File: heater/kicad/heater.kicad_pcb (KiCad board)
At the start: 2 copper layers, 90 x 88.4 mm, 82 parts, among them J1 Conn_01x02_Pin, J2 Conn_01x02_Pin, J3 pcie_98, U1 OPA863SIDBVR, U10 B0509XT-1WR3, U11 ESD5344D-TP, U12 ESD5344D-TP, U13 XC6206P332MR, U2 OPA863SIDBVR, U3 LTC1968, U4 LTC1968, U5 OPA863SIDBVR, U6 OPA863SIDBVR, U7 LP2985-5.0, U8 ADS1115IDGS, U9 ISO1541

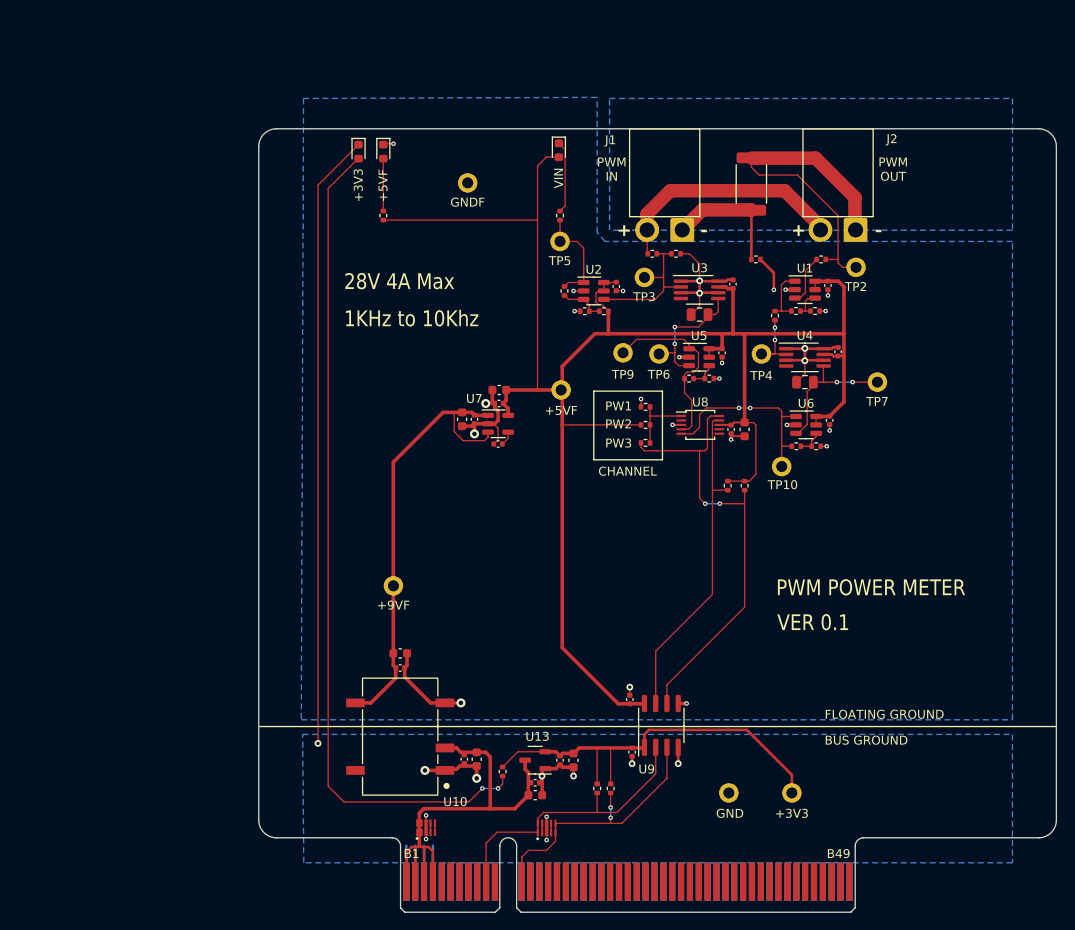
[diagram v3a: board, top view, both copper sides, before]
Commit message: Routed V2 of the heater board.
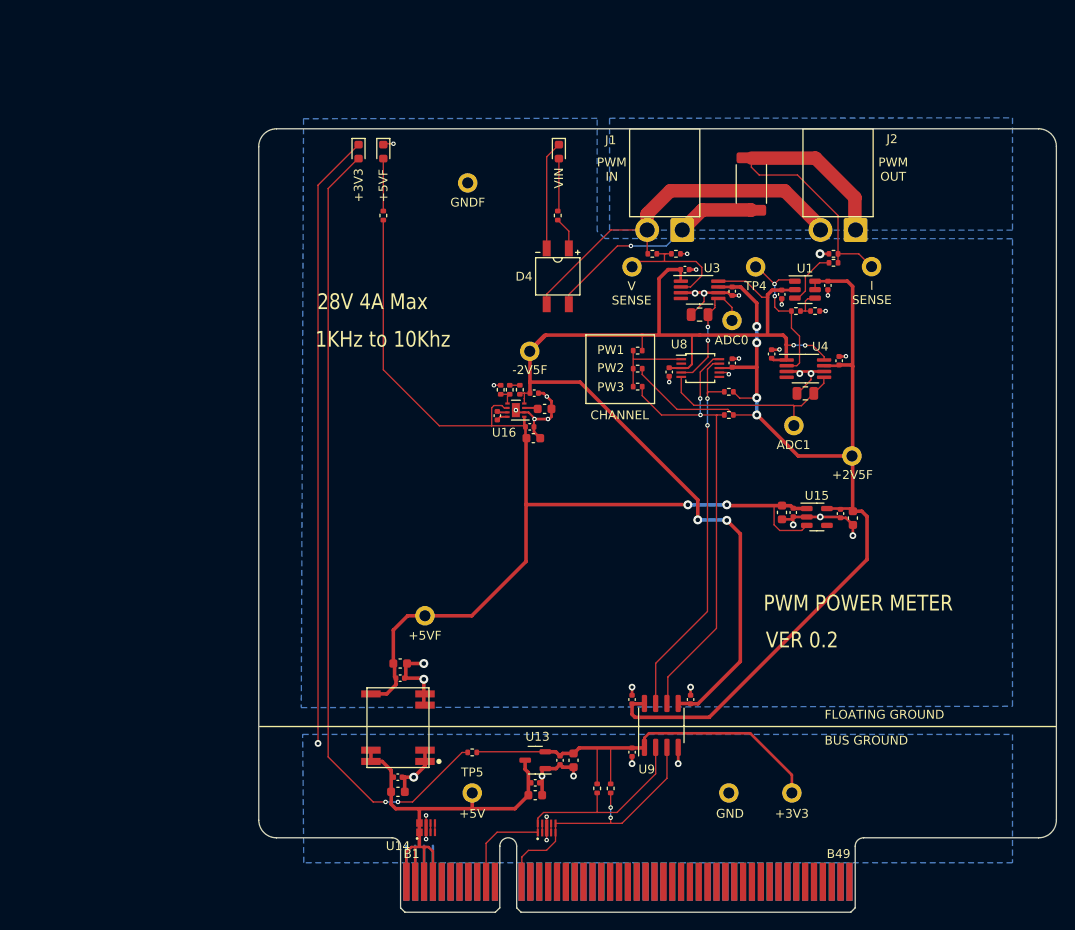
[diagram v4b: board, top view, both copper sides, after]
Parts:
- removed C10, C2: 100n, Capacitor_SMD:C_0402_1005Metric
- removed C11: 10n, Capacitor_SMD:C_0402_1005Metric
- removed C12: 10u, Capacitor_SMD:C_0603_1608Metric
- removed C14: 100n 16V, Capacitor_SMD:C_0402_1005Metric
- removed C15: 10u 16V, Capacitor_SMD:C_0603_1608Metric
- removed D2: RED, LED_SMD:LED_0603_1608Metric
- removed R11: 1M, Resistor_SMD:R_0402_1005Metric
- removed R13: 5K1, Resistor_SMD:R_0402_1005Metric
- removed R14, R16: 30K, Resistor_SMD:R_0402_1005Metric
- removed R15, R17: 10K, Resistor_SMD:R_0402_1005Metric
- removed R7: 50K, Resistor_SMD:R_0402_1005Metric
- removed R8: 2K, Resistor_SMD:R_0402_1005Metric
- removed TP10, TP9: TestPoint, common:Test_Pad
- removed U10: B0509XT-1WR3, heater:Converter_DCDC
- removed U2, U5, U6: OPA863SIDBVR, Package_TO_SOT_SMD:TSOT-23-6
- removed U7: LP2985-5.0, Package_TO_SOT_SMD:SOT-23-5
- added C26: 10u, Capacitor_SMD:C_0603_1608Metric, F.Cu at (38.9, -44.5)
- added C27: 100n, Capacitor_SMD:C_0402_1005Metric, F.Cu at (37.5, -45.0)
- added C28: 100n, Capacitor_SMD:C_0402_1005Metric, F.Cu at (32.2, -45.1)
- added C29: 10u, Capacitor_SMD:C_0603_1608Metric, F.Cu at (30.9, -45.1)
- added C30: 4u7, Capacitor_SMD:C_0603_1608Metric, F.Cu at (4.10, -56.8)
- added C31: 1u, Capacitor_SMD:C_0402_1005Metric, F.Cu at (2.93, -58.6)
- added C32: 1u, Capacitor_SMD:C_0402_1005Metric, F.Cu at (-1.23, -56.0)
- added C33: 10u, Capacitor_SMD:C_0603_1608Metric, F.Cu at (2.83, -53.5)
- added C34: 100n, Capacitor_SMD:C_0402_1005Metric, F.Cu at (2.42, -54.8)
- added C35: 100n, Capacitor_SMD:C_0402_1005Metric, F.Cu at (20.6, -24.0)
- added C37: 100n, Capacitor_SMD:C_0402_1005Metric, F.Cu at (18.2, -61.0)
- added D4: MBS10S, common:Diode_Bridge_MBS10, F.Cu at (5.59, -71.8)
- added D5: RED, LED_SMD:LED_0603_1608Metric, F.Cu at (5.71, -85.8)
- added R26: 200K, Resistor_SMD:R_0402_1005Metric, F.Cu at (1.31, -59.0)
- added R27: 200K, Resistor_SMD:R_0402_1005Metric, F.Cu at (-0.85, -59.0)
- added R28: 10K, Resistor_SMD:R_0402_1005Metric, F.Cu at (0.16, -59.0)
- added TP14: TestPoint, common:Test_Pad, F.Cu at (38.8, -51.5)
- added U14: B0505MT-1WR4, common:B0505MT-1WR4, F.Cu at (-12.4, -20.8)
- added U15: TPS7A2025PDBVR, Package_TO_SOT_SMD:SOT-23-5, F.Cu at (34.8, -44.6)
- added U16: LM27761, Package_SON:WSON-8-1EP_2x2mm_P0.5mm_EP0.9x1.6mm, F.Cu at (0.86, -56.7)
- C16: value 10u 16V -> 10u
- C17: value 100n 16V -> 100n
- C9: value 10u -> 100n; footprint Capacitor_SMD:C_0603_1608Metric -> Capacitor_SMD:C_0402_1005Metric
- R12: value 0R -> 10K
- R2: value 0R025 50ppm -> 0R025
- moved TP5 63.0 mm to (-4.06, -13.5)
- moved C9 33.7 mm to (30.9, -69.7), turned to -90 degrees
- moved R12 27.0 mm to (5.59, -78.6)
- moved TP3 25.7 mm to (41.0, -72.8)
- moved TP2 25.3 mm to (14.0, -72.8)
- moved TP7 10.6 mm to (32.2, -54.9)
- moved R21 10.6 mm to (24.9, -58.7), turned to 0 degrees
- moved C7 10.3 mm to (19.9, -72.5), turned to 0 degrees
- moved C8 9.95 mm to (29.7, -63.0), turned to 90 degrees
- moved TP4 9.85 mm to (27.9, -72.8)
- moved C22 9.62 mm to (-12.4, -13.6), turned to 180 degrees
- moved TP6 9.06 mm to (25.2, -66.8)
- moved R1 8.78 mm to (36.7, -74.3), turned to 180 degrees
- moved R22 8.17 mm to (24.9, -56.1), turned to 0 degrees
- moved C20 7.78 mm to (-12.5, -15.2), turned to 180 degrees
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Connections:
- net /VIN+ renamed /VIN2
- C1 pad 1: +5VF -> +2V5F
- C13 pad 1: +5VF -> GNDF
- C13 pad 2: GNDF -> +2V5F
- C16 pad 2: /9VF -> +5VF
- C17 pad 2: /9VF -> +5VF
- C18 pad 1: +5VF -> +2V5F
- C3 pad 1: +5VF -> +2V5F
- C4 pad 1: +5VF -> +2V5F
- C5 pad 2: Net-(U3-OUT) -> /ADC0
- C6 pad 2: Net-(U4-OUT) -> /ADC1
- C7 pad 1: +5VF -> -2V5F
- C8 pad 1: +5VF -> -2V5F
- C9 pad 1: GNDF -> -2V5F
- C9 pad 2: +5VF -> GNDF
- J1 pad 1: Net-(J1-Pin_1) -> /VIN1
- J2 pad 1: Net-(J2-Pin_1) -> /I_SENSE
- R1 pad 1: Net-(J1-Pin_1) -> /I_SENSE
- R12 pad 1: Net-(U4-IN1) -> Net-(D4-+)
- R12 pad 2: Net-(R12-Pad2) -> Net-(D5-A)
- R19 pad 2: GNDF -> -2V5F
- R2 pad 1: Net-(J1-Pin_1) -> /VIN1
- R2 pad 2: Net-(J2-Pin_1) -> /I_SENSE
- R20 pad 2: +5VF -> +2V5F
- R21 pad 2: +5VF -> +2V5F
- R22 pad 2: +5VF -> +2V5F
- R3 pad 1: Net-(U2--) -> /V_SENSE
- R4 pad 1: Net-(U2--) -> /V_SENSE
- R6 pad 1: Net-(J2-Pin_1) -> /I_SENSE
- R9 pad 1: Net-(R12-Pad2) -> Net-(U4-IN1)
- TP11 pad 1: /9VF -> +5VF
- TP2 pad 1: Net-(J2-Pin_1) -> /V_SENSE
- TP3 pad 1: Net-(U2--) -> /I_SENSE
- TP5 pad 1: Net-(R11-Pad2) -> +5V
- TP6 pad 1: Net-(U3-OUT) -> /ADC0
- TP7 pad 1: Net-(U4-OUT) -> /ADC1
- TP8 pad 1: +5VF -> -2V5F
- U1 pad 1: Net-(R12-Pad2) -> Net-(U4-IN1)
- U1 pad 2: GNDF -> -2V5F
- U1 pad 5: +5VF -> +2V5F
- U1 pad 6: +5VF -> +2V5F
- U3 pad 1: GNDF -> -2V5F
- U3 pad 2: Net-(U2--) -> /V_SENSE
- U3 pad 5: Net-(U3-OUT) -> /ADC0
- U3 pad 7: +5VF -> +2V5F
- U3 pad 8: GNDF -> -2V5F
- U4 pad 1: GNDF -> -2V5F
- U4 pad 5: Net-(U4-OUT) -> /ADC1
- U4 pad 7: +5VF -> +2V5F
- U4 pad 8: GNDF -> -2V5F
- U8 pad 3: GNDF -> -2V5F
- U8 pad 4: Net-(U8-AIN0) -> /ADC0
- U8 pad 5: Net-(U8-AIN1) -> /ADC1
- U8 pad 7: unconnected-(U8-AIN3-Pad7) -> GNDF
- U8 pad 8: +5VF -> +2V5F
- U9 pad 5: GNDF -> -2V5F
- U9 pad 8: +5VF -> +2V5F
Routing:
- net -2V5F: track 0.00 -> 137.3 mm, vias 0 -> 4
- net +2V5F: track 0.00 -> 133.4 mm, vias 0 -> 4
- net +5VF: track 208.8 -> 121.5 mm, vias 0 -> 2
- net /9VF: track 50.5 -> 0.00 mm
- net /I_SENSE: track 0.00 -> 40.0 mm
- net Net-(J2-Pin_1): track 39.2 -> 0.00 mm
- net /VIN1: track 0.00 -> 25.7 mm, vias 0 -> 1
- net /ADC1: track 0.00 -> 22.5 mm
- net Net-(U8-AIN1): track 22.2 -> 0.00 mm, vias 2 -> 0
- net Net-(U8-AIN0): track 21.1 -> 0.00 mm
- net GNDF: track 78.0 -> 59.6 mm, vias 26 -> 29
- net Net-(U2--): track 17.1 -> 0.00 mm
- net /VIN2: track 27.2 -> 42.6 mm
- net Net-(U4-OUT): track 15.4 -> 0.00 mm, vias 2 -> 0
- net /V_SENSE: track 0.00 -> 14.8 mm
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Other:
- board text added: "+2V5F"
- board text added: "+5V"
- board text added: "-2V5F"
- board text added: "ADC0"
- board text added: "ADC1"
- board text added: "ASC1"
- board text added: "I SENSE"
- board text added: "V SENSE"
- board text added: "VER 0.2"
- board text removed: "+"
- board text removed: "+9VF"
- board text removed: "-"
- board text removed: "TO9"
- board text removed: "TP10"
- board text removed: "TP2"
- board text removed: "TP3"
- board text removed: "TP5"
- board text removed: "TP6"
- board text removed: "TP7"
- board text removed: "TP9"
- board text removed: "VER 0.1"

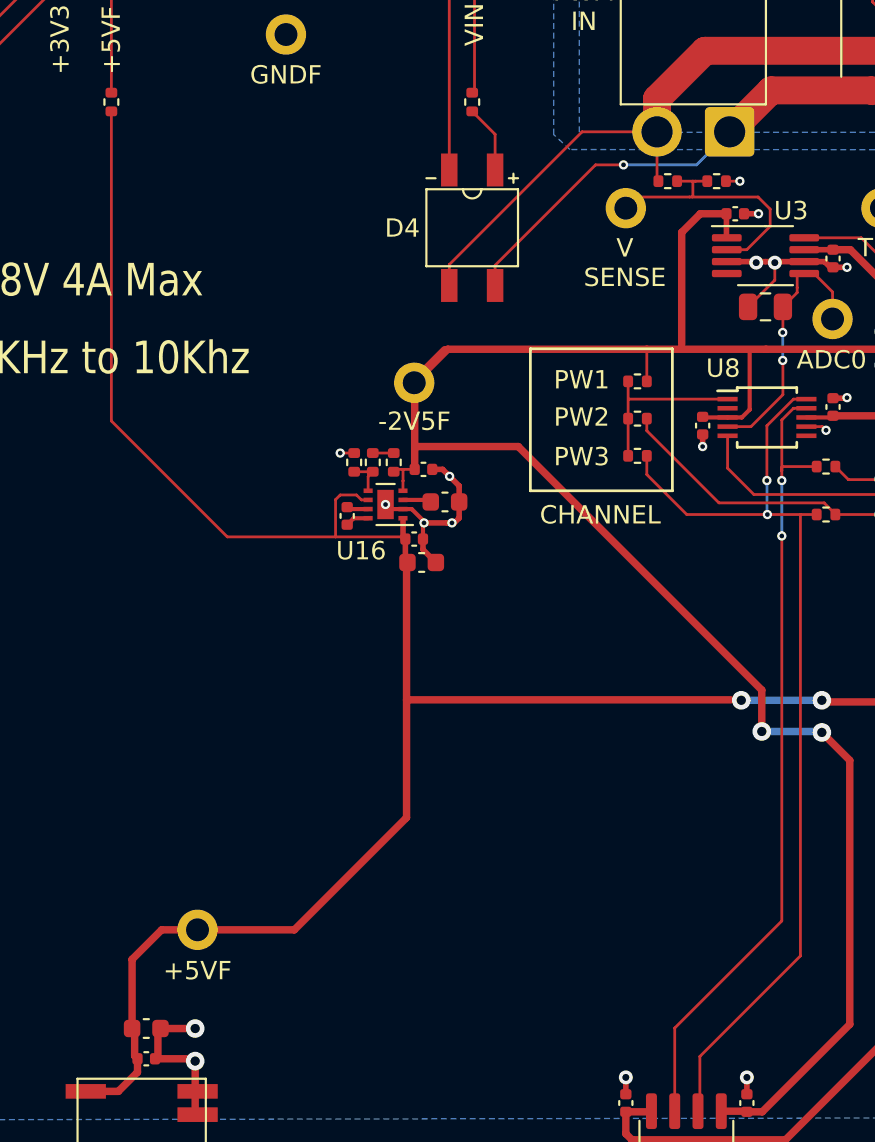
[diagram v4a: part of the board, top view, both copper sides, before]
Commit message: Updated heater schematic.
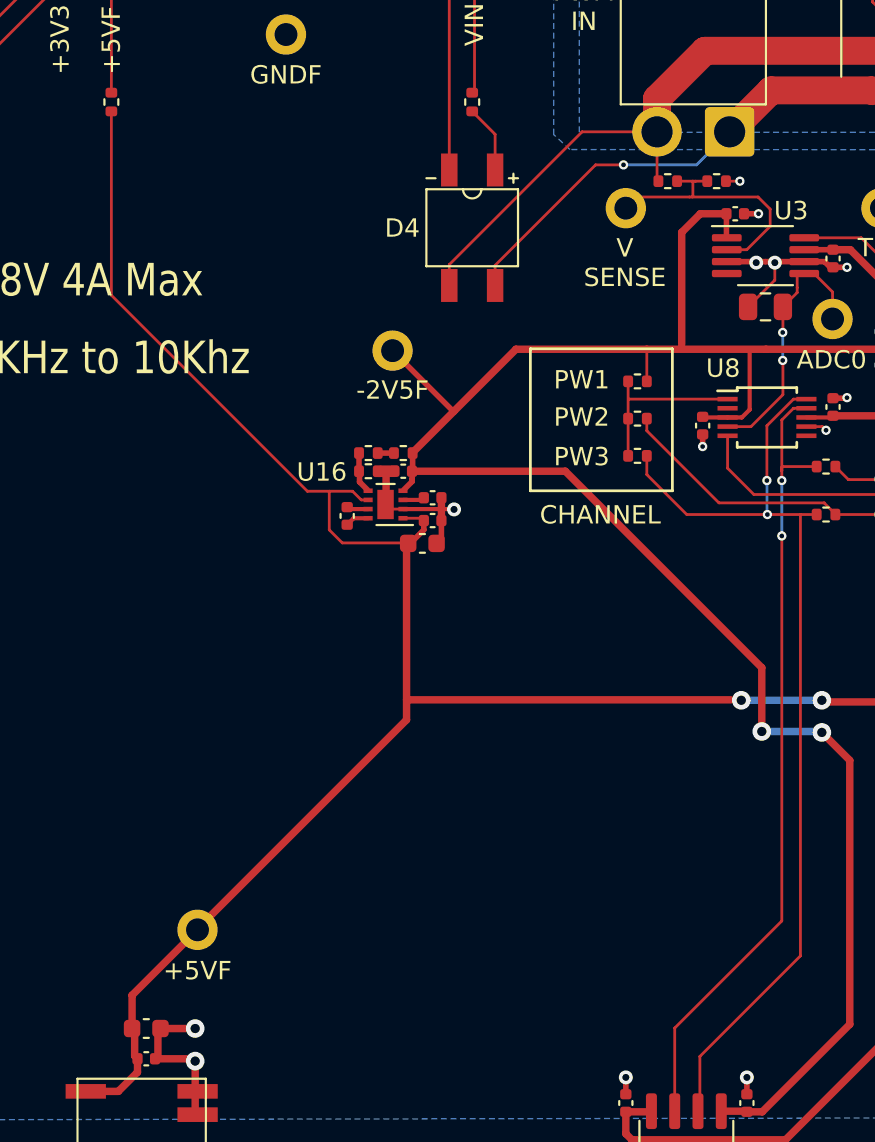
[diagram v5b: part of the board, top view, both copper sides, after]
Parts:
- C30: footprint Capacitor_SMD:C_0603_1608Metric -> Capacitor_SMD:C_0402_1005Metric
- moved TP8 2.11 mm to (1.24, -65.0)
- moved C34 1.42 mm to (3.43, -55.8)
- moved C31 1.11 mm to (1.83, -58.5), turned to 0 degrees
- moved C33 1.04 mm to (2.87, -54.5)
- moved R27 0.91 mm to (-0.08, -58.5), turned to 0 degrees
- moved R26 0.73 mm to (1.83, -59.5), turned to 180 degrees
- moved C30 0.71 mm to (3.43, -57.0)
- moved R28 0.56 mm to (-0.08, -59.5), turned to 180 degrees
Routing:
- net +5VF: track 121.5 -> 114.4 mm
- net Net-(U16-CPOUT): track 1.56 -> 0.98 mm
- net -2V5F: track 137.3 -> 136.8 mm
- net GNDF: track 59.6 -> 59.1 mm, vias 29 -> 25

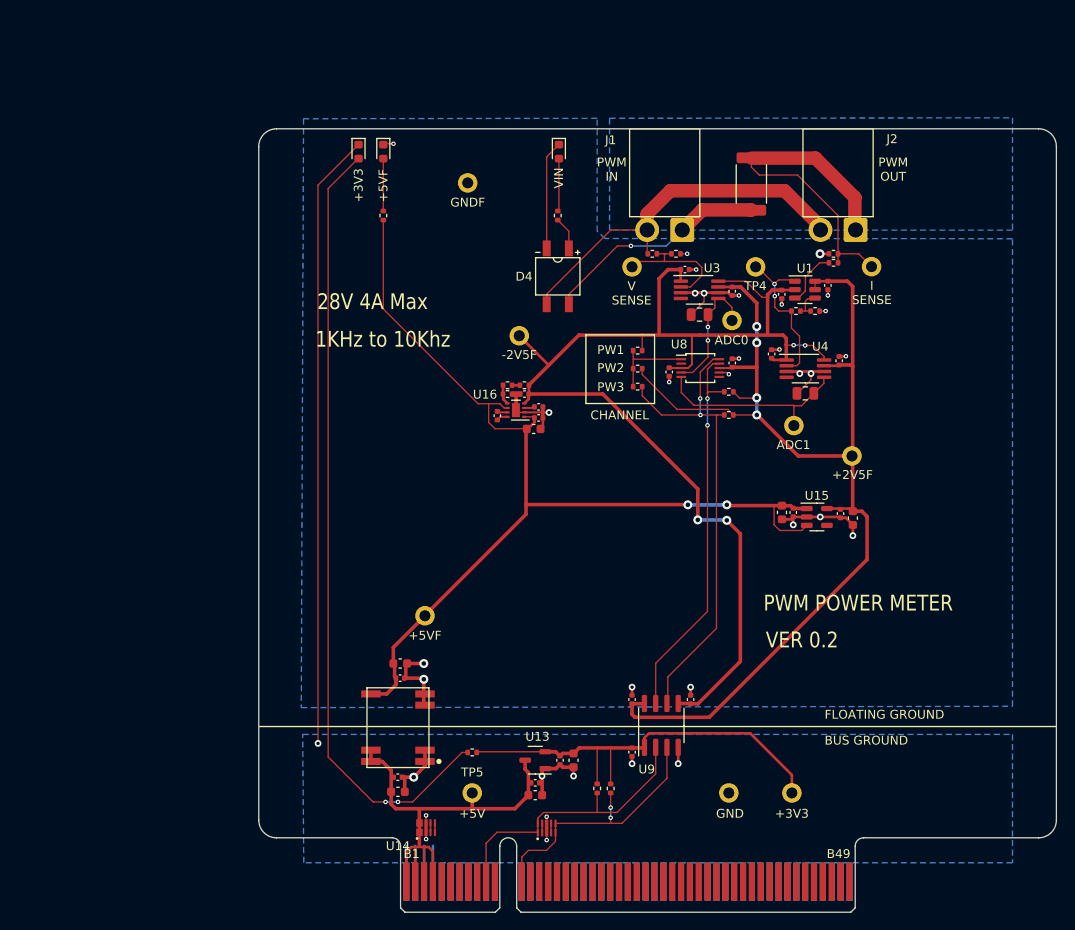
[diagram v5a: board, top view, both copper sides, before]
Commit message: Updated the heater schematic. Using +/-5V dc/dc instead of a charge pump.
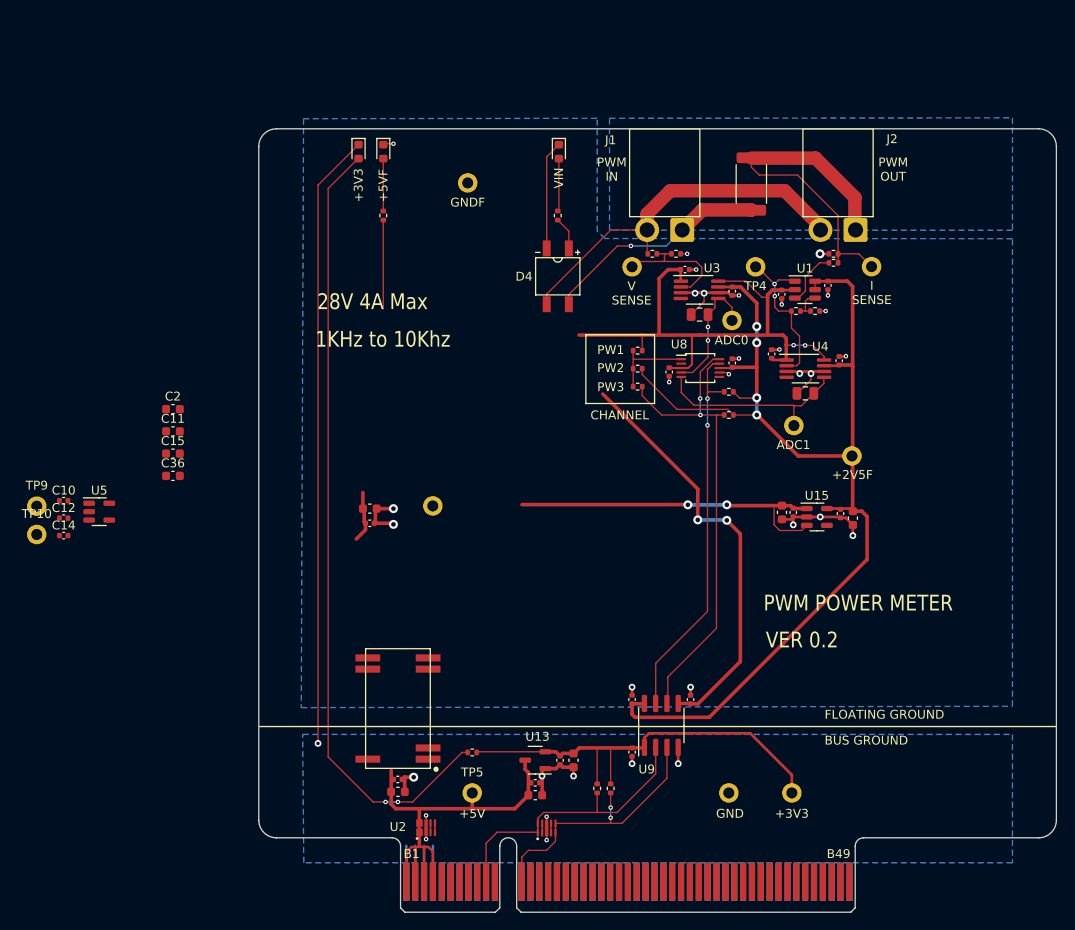
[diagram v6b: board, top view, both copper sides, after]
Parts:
- removed C30: 4u7, Capacitor_SMD:C_0402_1005Metric
- removed C31, C32: 1u, Capacitor_SMD:C_0402_1005Metric
- removed C33: 10u, Capacitor_SMD:C_0603_1608Metric
- removed C34: 100n, Capacitor_SMD:C_0402_1005Metric
- removed R26, R27: 200K, Resistor_SMD:R_0402_1005Metric
- removed R28: 10K, Resistor_SMD:R_0402_1005Metric
- removed TP8: TestPoint, common:Test_Pad
- removed U14: B0505MT-1WR4, common:B0505MT-1WR4
- removed U16: LM27761, Package_SON:WSON-8-1EP_2x2mm_P0.5mm_EP0.9x1.6mm
- added C10: 100n, Capacitor_SMD:C_0402_1005Metric, F.Cu at (-50.2, -46.4)
- added C11: 10u, Capacitor_SMD:C_0603_1608Metric, F.Cu at (-37.8, -54.3)
- added C12: 100n, Capacitor_SMD:C_0402_1005Metric, F.Cu at (-50.2, -44.5)
- added C14: 100n, Capacitor_SMD:C_0402_1005Metric, F.Cu at (-50.2, -42.5)
- added C15: 10u, Capacitor_SMD:C_0603_1608Metric, F.Cu at (-37.8, -51.7)
- added C2: 10u, Capacitor_SMD:C_0603_1608Metric, F.Cu at (-37.8, -56.8)
- added C36: 10u, Capacitor_SMD:C_0603_1608Metric, F.Cu at (-37.8, -49.2)
- added TP10: TestPoint, common:Test_Pad, F.Cu at (-53.2, -42.6)
- added TP9: TestPoint, common:Test_Pad, F.Cu at (-53.2, -45.8)
- added U2: D050505T-1WR4, common:D050505T-1WR4, F.Cu at (-12.4, -23.0)
- added U5: TPS72325DBVR, Package_TO_SOT_SMD:SOT-23-5, F.Cu at (-46.2, -45.2)
- moved C16 17.8 mm to (-15.6, -45.5)
- moved C17 17.8 mm to (-15.6, -43.9)
- moved TP11 12.4 mm to (-8.51, -45.8)
- moved C20 0.25 mm to (-12.5, -15.0)
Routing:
- net +5VF: track 114.4 -> 53.9 mm
- net -2V5F: track 136.8 -> 113.4 mm
- net GNDF: track 59.1 -> 45.3 mm, vias 25 -> 24
- net +5V: track 52.6 -> 48.6 mm
- net GND: track 107.7 -> 104.2 mm
- net Net-(U16-VFB): track 2.21 -> 0.00 mm
- net Net-(U16-C+): track 1.29 -> 0.00 mm
- net Net-(U16-C-): track 1.19 -> 0.00 mm
- net Net-(U16-CPOUT): track 0.98 -> 0.00 mm
- net Net-(R26-Pad2): track 0.89 -> 0.00 mm
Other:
- board text removed: "-2V5F"
